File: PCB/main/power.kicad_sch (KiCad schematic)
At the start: 0 parts

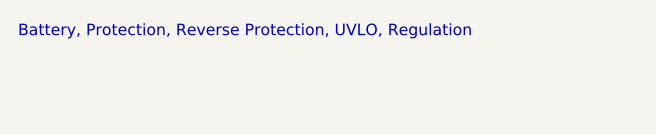
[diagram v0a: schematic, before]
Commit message: Added sheet details to schematic
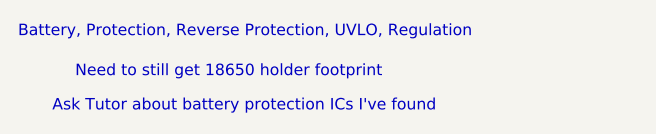
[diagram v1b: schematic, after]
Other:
- note added: "Ask Tutor about battery protection ICs I've found"
- note added: "Need to still get 18650 holder footprint"
- company: (none) -> UCT
- title: (none) -> Power Module for STMDiscovery HAT
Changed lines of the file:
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@@
 (kicad_sch (version 20211123) (generator eeschema)
   (paper "A4")
+  (title_block
+    (title "Power Module for STMDiscovery HAT")
+    (date "2022-03-02")
+    (rev "v0.0")
+    (company "UCT")
+    (comment 1 "Ryan Jones")
+    (comment 2 "Group 7")
+    (comment 3 "@Checked By: ")
+    (comment 4 "@Authors: Ryan Jones, Alex Cargill & Devlin Trafford")
+  )
+  (text "Ask Tutor about battery protection ICs I've found" (at 125.73 97.79 0)
+    (effects (font (size 1.27 1.27)) (justify left bottom))
+  )
   (text "Battery, Protection, Reverse Protection, UVLO, Regulation"
     (at 121.92 89.535 0)
     (effects (font (size 1.27 1.27)) (justify left bottom))
   )
+  (text "Need to still get 18650 holder footprint" (at 128.27 93.98 0)
+    (effects (font (size 1.27 1.27)) (justify left bottom))
+  )

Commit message: Add Power Module Datasheets
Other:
- note added: "UVLO - LM1117-3.3 Battery Charger - TP4056 Input Voltage Polarity Protection - Diode w/ Voltage Divider (to set ref. voltage) after USB, before Charging IC Battery Polarity Protection - FET after Battery in Parallel Regulation - What do we need to regulate? Input charging voltage? Or Output (3.3V)? Or both?"
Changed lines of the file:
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@@
     (comment 4 "@Authors: Ryan Jones, Alex Cargill & Devlin Trafford")
+  )
+  (text "UVLO - LM1117-3.3\nBattery Charger - TP4056\nInput Voltage Polarity Protection - Diode w/ Voltage Divider (to set ref. voltage) after USB, before Charging IC\nBattery Polarity Protection - FET after Battery in Parallel\nRegulation - What do we need to regulate? Input charging voltage? Or Output (3.3V)? Or both?"
+    (at 116.84 110.49 0)
+    (effects (font (size 1.27 1.27)) (justify left bottom))
   )
   (text "Ask Tutor about battery protection ICs I've found" (at 125.73 97.79 0)

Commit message: Power Module v0.01
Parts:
- added 0.4Ω, 1kΩ (x2), R?: R, symbol Device:R_Small_US
- added BT?: 18650 Battery, symbol Device:Battery_Cell
- added C? (x2): 10uF, symbol Device:C_Small
- added D?: Red LED, symbol Device:LED
- added D?: Green LED, symbol Device:LED
- added IC?: TP4056-42-ESOP8, SOIC127P600X175-9N, symbol TP4056:TP4056-42-ESOP8
- added J?: Conn_01x33_Female, Connector_PinHeader_2.54mm:PinHeader_1x33_P2.54mm_Vertical, symbol Connector:Conn_01x33_Female
- added J?: Conn_01x33_Female, Connector_PinSocket_2.54mm:PinSocket_1x33_P2.54mm_Vertical, symbol Connector:Conn_01x33_Female
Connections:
- new net: 1kΩ.1, D?.1 (K) (x2)
- new net: 0.4Ω.2, C?.1, D?.2 (A), D?.2 (A), IC?.4 (VCC), IC?.8 (CE)
- new net: 1kΩ.2, IC?.6 (~{STDBY})
- new net: 1kΩ.2, IC?.7 (~{CHRG})
- new net: IC?.2 (PROG), R?.1
- new net +5V: 0.4Ω.1, J?.1 (Pin_1), J?.1 (Pin_1)
- new net BAT +: BT?.1 (+), C?.1, IC?.5 (BAT)
- new net BOOT: J?.6 (Pin_6), J?.6 (Pin_6)
- new net GND: BT?.2 (-), C?.2, C?.2, IC?.1 (TEMP), IC?.3 (GND), J?.2 (Pin_2), J?.2 (Pin_2), J?.33 (Pin_33), J?.33 (Pin_33), R?.2
- new net PA10: J?.23 (Pin_23), J?.23 (Pin_23)
- new net PA11: J?.22 (Pin_22), J?.22 (Pin_22)
- new net PA12: J?.21 (Pin_21), J?.21 (Pin_21)
- new net PA13: J?.20 (Pin_20), J?.20 (Pin_20)
- new net PA14: J?.17 (Pin_17), J?.17 (Pin_17)
- new net PA15: J?.16 (Pin_16), J?.16 (Pin_16)
- new net PA8: J?.25 (Pin_25), J?.25 (Pin_25)
- new net PA9: J?.24 (Pin_24), J?.24 (Pin_24)
- new net PB13: J?.32 (Pin_32), J?.32 (Pin_32)
- new net PB14: J?.31 (Pin_31), J?.31 (Pin_31)
- new net PB15: J?.30 (Pin_30), J?.30 (Pin_30)
- new net PB3: J?.11 (Pin_11), J?.11 (Pin_11)
- new net PB4: J?.10 (Pin_10), J?.10 (Pin_10)
- new net PB5: J?.9 (Pin_9), J?.9 (Pin_9)
- new net PB6: J?.8 (Pin_8), J?.8 (Pin_8)
- new net PB7: J?.7 (Pin_7), J?.7 (Pin_7)
- new net PB8: J?.4 (Pin_4), J?.4 (Pin_4)
- new net PB9: J?.3 (Pin_3), J?.3 (Pin_3)
- new net PC10: J?.15 (Pin_15), J?.15 (Pin_15)
- new net PC11: J?.14 (Pin_14), J?.14 (Pin_14)
- new net PC12: J?.13 (Pin_13), J?.13 (Pin_13)
- new net PC6: J?.29 (Pin_29), J?.29 (Pin_29)
- new net PC7: J?.28 (Pin_28), J?.28 (Pin_28)
- new net PC8: J?.27 (Pin_27), J?.27 (Pin_27)
- new net PC9: J?.26 (Pin_26), J?.26 (Pin_26)
- new net PD2: J?.12 (Pin_12), J?.12 (Pin_12)
- new net PF6: J?.19 (Pin_19), J?.19 (Pin_19)
- new net PF7: J?.18 (Pin_18), J?.18 (Pin_18)
- new net VDD: J?.5 (Pin_5), J?.5 (Pin_5)
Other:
- note added: "16 units apart = 2.54 x 16"

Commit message: Power Module v0.01
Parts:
- added 10kΩ, 10kΩ? (x2), 1kΩ? (x7): R, symbol Device:R_Small_US
- added C? (x3): C_Small, symbol Device:C_Small
- added D?: D_Zener, symbol Device:D_Zener
- added D? (x2): 1N4007, Diode_THT:D_DO-41_SOD81_P10.16mm_Horizontal, symbol Diode:1N4007
- added D?: MBR0540, Diode_SMD:D_SOD-123, symbol Diode:MBR0540
- added IC?: AMS1117-3.3, SOT229P700X180-4N, symbol AMS1117-3.3V:AMS1117-3.3
- added Q?: Q_PNP_BCE, symbol Device:Q_PNP_BCE
- added Q?: Q_NMOS_DSG, symbol Device:Q_NMOS_DSG
- added Q?: BC857, Package_TO_SOT_SMD:SOT-23, symbol Transistor_BJT:BC857
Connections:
- net +5V: now also Q?.2 (C); no longer 0.4Ω.1
- net BAT +: now also D?.2 (A), Q?.3 (G)
- net GND: now also 10kΩ.2, 10kΩ?.2, 1kΩ?.2, 1kΩ?.2, C?.2, C?.2, C?.2, Q?.2 (S)
- new net: 10kΩ?.1, 10kΩ?.2, IC?.1 (GND/ADJ)
- new net: 10kΩ.1, Q?.1 (B)
- new net: 1kΩ?.1, 1kΩ?.2
- new net: 1kΩ?.1, 1kΩ?.2, Q?.2 (E)
- new net: 1kΩ?.1, 1kΩ?.2, C?.1, Q?.1 (B)
- new net: 1kΩ?.1, 1kΩ?.1, Q?.3 (C)
- new net: 1kΩ?.1, 1kΩ?.1, 1kΩ?.2
- new net: 1kΩ?.2, C?.1, D?.1 (K)
- new net 5V_Power: C?.1, D?.1 (K), IC?.3 (VIN)
- new net OUT: D?.1 (K), D?.1 (K)
- new net VPolarity: 0.4Ω.1, D?.2 (A), Q?.3 (E)
- new net VRegulated: 10kΩ?.1, D?.2 (A), IC?.2 (VOUT)
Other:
- note added: "Battery Polarity Protection"
- note added: "Input Polarity Protection Circuit"
- note added: "Load"
- note added: "Power from the USB when powering the HAT using laptop power instead of battery (Need a switch system)"
- note added: "SW"
- note added: "TP4056 - LI-Ion Battery Charger"
- note added: "To voltage regulator"
- note added: "Vin"
- note added: "Voltage Regulation"
- note added: "Vshdown"
- note removed: "Ask Tutor about battery protection ICs I've found"
- moved on the sheet: 0.4Ω, 1kΩ, BT?, C?, D?, IC?, R?

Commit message: Power Module v0.02
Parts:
- removed D? (x2): 1N4007, Diode_THT:D_DO-41_SOD81_P10.16mm_Horizontal, symbol Diode:1N4007
- added J7: MICROXNJ, MICROXNJ, symbol MICROXNJ:MICROXNJ
- added Q4: Q_PMOS_GDS, symbol Device:Q_PMOS_GDS
- added Q5: 2N3904, Package_TO_SOT_THT:TO-92_Inline, symbol Transistor_BJT:2N3904
- added R3, R5, R8: 10kΩ, symbol Device:R_Small_US
- added U1: LM393, symbol Comparator:LM393
- R10, R9: renamed from 10kΩ?; value R -> 10kΩ
- R11, R12, R13, R14, R15, R16: renamed from 1kΩ?; value R -> 1kΩ
- R2: renamed from 0.4Ω; value R -> 0.4Ω
- R4: renamed from 10kΩ; value R -> 10kΩ
- R6, R7: renamed from 1kΩ; value R -> 1kΩ
- gave numbers to parts that had none: 19
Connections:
- net GND: now also J7.5, J7.MH1, J7.MH2, J7.MH3, J7.MH4, J7.MP1, J7.MP2, Q5.1 (E)
- net VPolarity: no longer R2.1
- net 5V_Power renamed 5VSupply
- net 5VSupply: now also Q4.3 (S), R3.1, R5.1, U1.2 (-)
- new net: Q5.2 (B), R8.2
- new net: Q4.1 (G), Q5.3 (C), R5.2
- new net ChargeEN: R2.1, R8.1
- new net ChargeOut: U1.1
- new net D+: J7.3
- new net D-: J7.2
- new net VCCBus: J7.1, Q4.2 (D), R3.2, U1.3 (+)
- no-connect marks 0 -> 1
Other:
- note added: "USB Detection"
- note added: "USB Input"
- note added: "UVLO"
- note added: "Under Voltage Cutout Protection"
- note removed: "Battery, Protection, Reverse Protection, UVLO, Regulation"
- note removed: "To voltage regulator"
- note removed: "UVLO - LM1117-3.3 Battery Charger - TP4056 Input Voltage Polarity Protection - Diode w/ Voltage Divider (to set ref. voltage) after USB, before Charging IC Battery Polarity Protection - FET after Battery in Parallel Regulation - What do we need to regulate? Input charging voltage? Or Output (3.3V)? Or both?"
- moved on the sheet: J5, J6

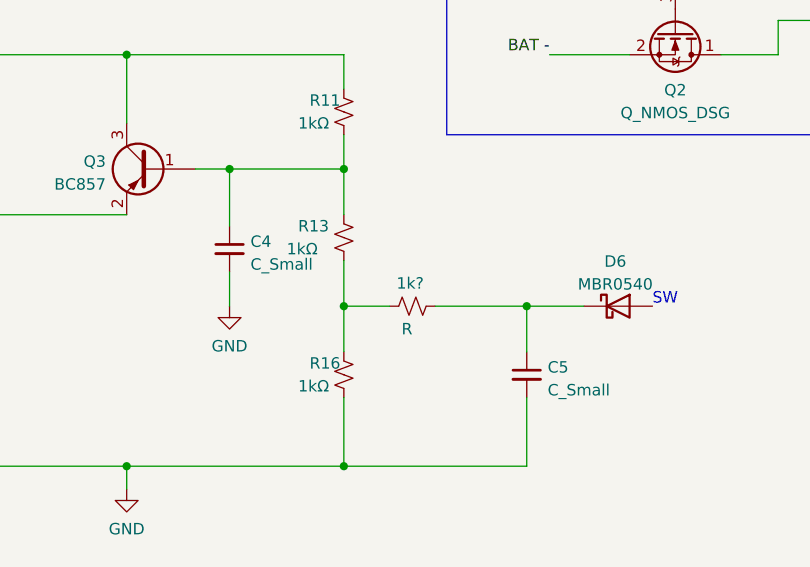
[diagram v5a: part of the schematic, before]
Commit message: Power module v0.02 update
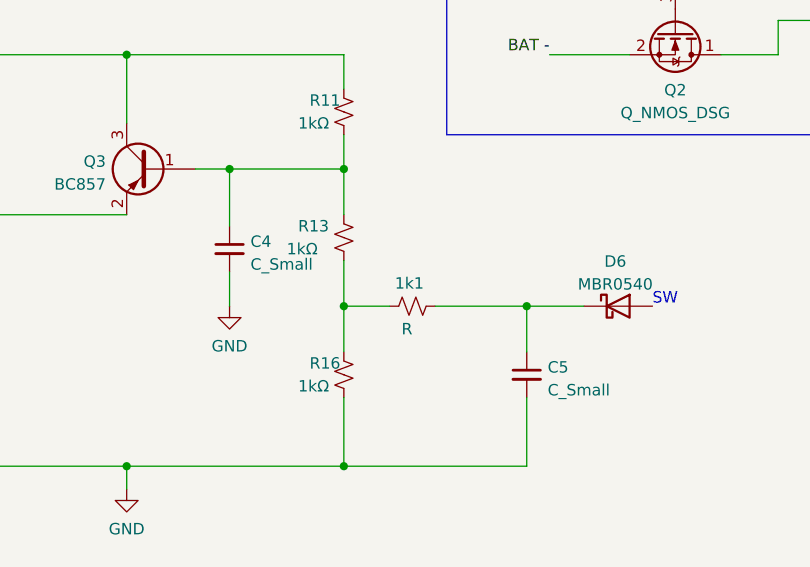
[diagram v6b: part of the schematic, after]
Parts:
- gave numbers to parts that had none: 1
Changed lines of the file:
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@@
   (symbol (lib_id "Device:R_Small_US") (at 229.87 130.81 90) (unit 1)
     (in_bom yes) (on_board yes)
-    (property "Reference" "1k?" (id 0) (at 231.14 128.27 90)
+    (property "Reference" "1k1" (id 0) (at 231.14 128.27 90)
       (effects (font (size 1.27 1.27)) (justify left))
     )

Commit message: Power Module v0.03
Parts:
- removed J5: Conn_01x33_Female, Connector_PinSocket_2.54mm:PinSocket_1x33_P2.54mm_Vertical, symbol Connector:Conn_01x33_Female
- removed J6: Conn_01x33_Female, Connector_PinHeader_2.54mm:PinHeader_1x33_P2.54mm_Vertical, symbol Connector:Conn_01x33_Female
- removed J7: MICROXNJ, MICROXNJ, symbol MICROXNJ:MICROXNJ
- added J?: MICROXNJ, MICROXNJ, symbol MICROXNJ:MICROXNJ
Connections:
- net +5V is gone; now on net VCCBus: Q1.2 (C)
- net D+: now also J?.3
- net D-: now also J?.2
- net GND: now also J?.5, J?.MH1, J?.MH2, J?.MH3, J?.MH4, J?.MP1, J?.MP2
- net VCCBus: now also J?.1; no longer Q4.2 (D), R3.2, U1.3 (+)
- net VPolarity: now also Q4.2 (D), R3.2, U1.3 (+)
- no-connect marks 1 -> 2
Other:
- note removed: "16 units apart = 2.54 x 16"
- moved on the sheet: 1k1, BT1, C1, C2, C4, C5, D3, D4, D6, IC1, Q2, Q3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

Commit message: Power Module v0.04 Update
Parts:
- removed 1k1: R, symbol Device:R_Small_US
- removed C4, C5: C_Small, symbol Device:C_Small
- removed D6: MBR0540, Diode_SMD:D_SOD-123, symbol Diode:MBR0540
- removed Q2: Q_NMOS_DSG, symbol Device:Q_NMOS_DSG
- removed Q3: BC857, Package_TO_SOT_SMD:SOT-23, symbol Transistor_BJT:BC857
- removed R12: 1kΩ, symbol Device:R_Small_US
- added D4: White LED, symbol Device:LED
- added D5: D_Zener, symbol Device:D_Zener
- added IC3: 74HC04D,653, SOIC127P600X175-14N, symbol 74HC04D-653:74HC04D,653
- added M1, M2: MPMOS, symbol pspice:MPMOS
- added M3, M4: MNMOS, symbol pspice:MNMOS
- added Q3: Q_PMOS_DGS, symbol Device:Q_PMOS_DGS
- added Q5: Q_NMOS_DSG, symbol Device:Q_NMOS_DSG
- added R10: 1kΩ, symbol Device:R_Small_US
- added U2: LT1492, symbol Amplifier_Operational:LT1492
- gave numbers to parts that had none: 1
- renumbered D3 to D1, D4 to D2, D5 to D3, Q4 to Q2, Q5 to Q4, R2 to R1, R8 to R12, R4 to R2, R6 to R3, R7 to R4, R1 to R5, R3 to R6, R9 to R7, R10 to R8, R5 to R9
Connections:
- net 5VSupply: now also IC3.14 (VCC), M1.3 (S), M1.4 (B), M2.2 (G), M2.3 (S), M2.4 (B), M4.2 (G)
- net BAT +: now also R11.1, Q3.3 (S), Q5.1 (D), Q5.3 (G), R10.1
- net GND: now also R14.2, D4.1 (K), IC3.7 (GND), M3.4 (B), M4.3 (S), M4.4 (B), Q5.2 (S); no longer R15.2
- net at R15.1: now also R13.2; no longer R14.2
- net at R14.1: now also R10.2, U2.2 (-)
- net at R13.1: now also Q3.2 (G), U2.1; no longer R11.2
- net at R16.1: now also R15.2, D5.2 (A); no longer R13.2
- net ChargeEN renamed INVOUT
- net INVOUT: now also IC3.2 (1Y); no longer R12.1
- net ChargeOut: no longer names the net of U1.1
- net ChargeOut: now also D4.2 (A)
- new net: M3.3 (S), M4.1 (D)
- new net: D5.1 (K), R11.2, U2.3 (+)
- new net ANDOUT: IC3.1 (1A), M1.1 (D), M2.1 (D), M3.1 (D)
- new net POWEROUT: Q3.1 (D)
- new net USBDETECT: M1.2 (G), M3.2 (G), R12.1
- no-connect marks 2 -> 12
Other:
- note added: "AND Gate for Charging Logic"
- note added: "Inverter for Charger"
- note added: "UVLO - NOT SURE IF CORRECT"
- note added: "Under Voltage Cutout Protection (Still need to update R values)"
- note removed: "Load"
- note removed: "SW"
- note removed: "UVLO"
- note removed: "Under Voltage Cutout Protection"
- note removed: "Vin"
- note removed: "Vshdown"
